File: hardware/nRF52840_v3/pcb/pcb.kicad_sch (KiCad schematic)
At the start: 151 parts, among them SW1 SW_DIP_x01, SW2 SW_DIP_x01, Y1 32.768 kHz

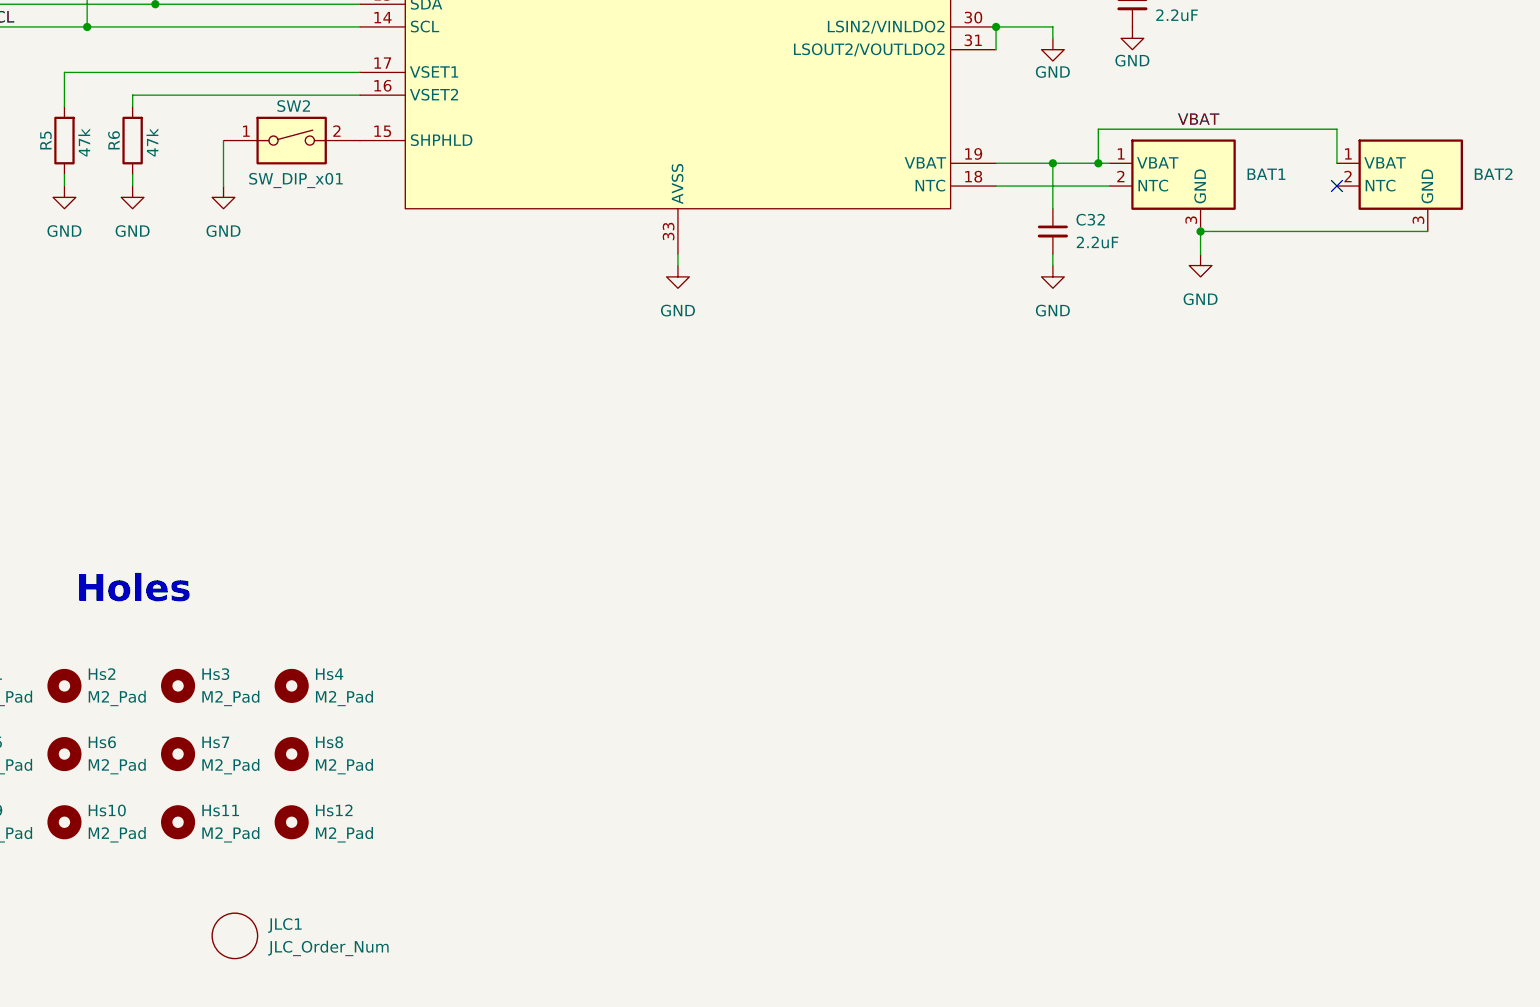
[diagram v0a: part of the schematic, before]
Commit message: M  hardware/nRF52840_v2/plate/plate.kicad_pcb M  hardware/nRF52840_v2/plate/plate.kicad_prl M  hardware/nRF52840_v2/plate/plate.kicad_pro A  hardware/nRF52840_v2/tmr-footprints/MountingHole_1.8mm_M1.6_NoPad.kicad_mod A  hardware/nRF52840_v2/tmr-footprints/MountingHole_2.2mm_M2.kicad_mod A  hardware/nRF52840_v2/tmr-footprints/SMTSO_M2.kicad_mod M  hardware/nRF52840_v3/border.py M  hardware/nRF52840_v3/pcb/pcb.kicad_pcb M  hardware/nRF52840_v3/pcb/pcb.kicad_prl M  hardware/nRF52840_v3/pcb/pcb.kicad_sch M  hardware/nRF52840_v3/placefp.py R  hardware/nRF52840_v2/plate/plate-Edge_Cuts.dxf -> hardware/nRF52840_v3/plate/plate-Edge_Cuts.dxf M  hardware/nRF52840_v3/plate/plate.kicad_pcb M  hardware/nRF52840_v3/plate/plate.kicad_prl M  hardware/nRF52840_v3/plate/plate.kicad_pro M  hardware/nRF52840_v3/plate/plate.kicad_sch A  hardware/nRF52840_v3/tmr-footprints/Aliexpress_SW_TACT_4x4x1.5mm.kicad_mod A  hardware/nRF52840_v3/tmr-footprints/MountingHole_1.8mm_M1.6_NoPad.kicad_mod A  hardware/nRF52840_v3/tmr-footprints/SMTSO_M2.kicad_mod M  hardware/nRF52840_v3/tmr-footprints/Stabilizer_Lowpro_2U.kicad_mod A  hardware/nRF52840_v3/tmr-footprints/USB_C_Receptacle_GCT_USB4085.kicad_mod
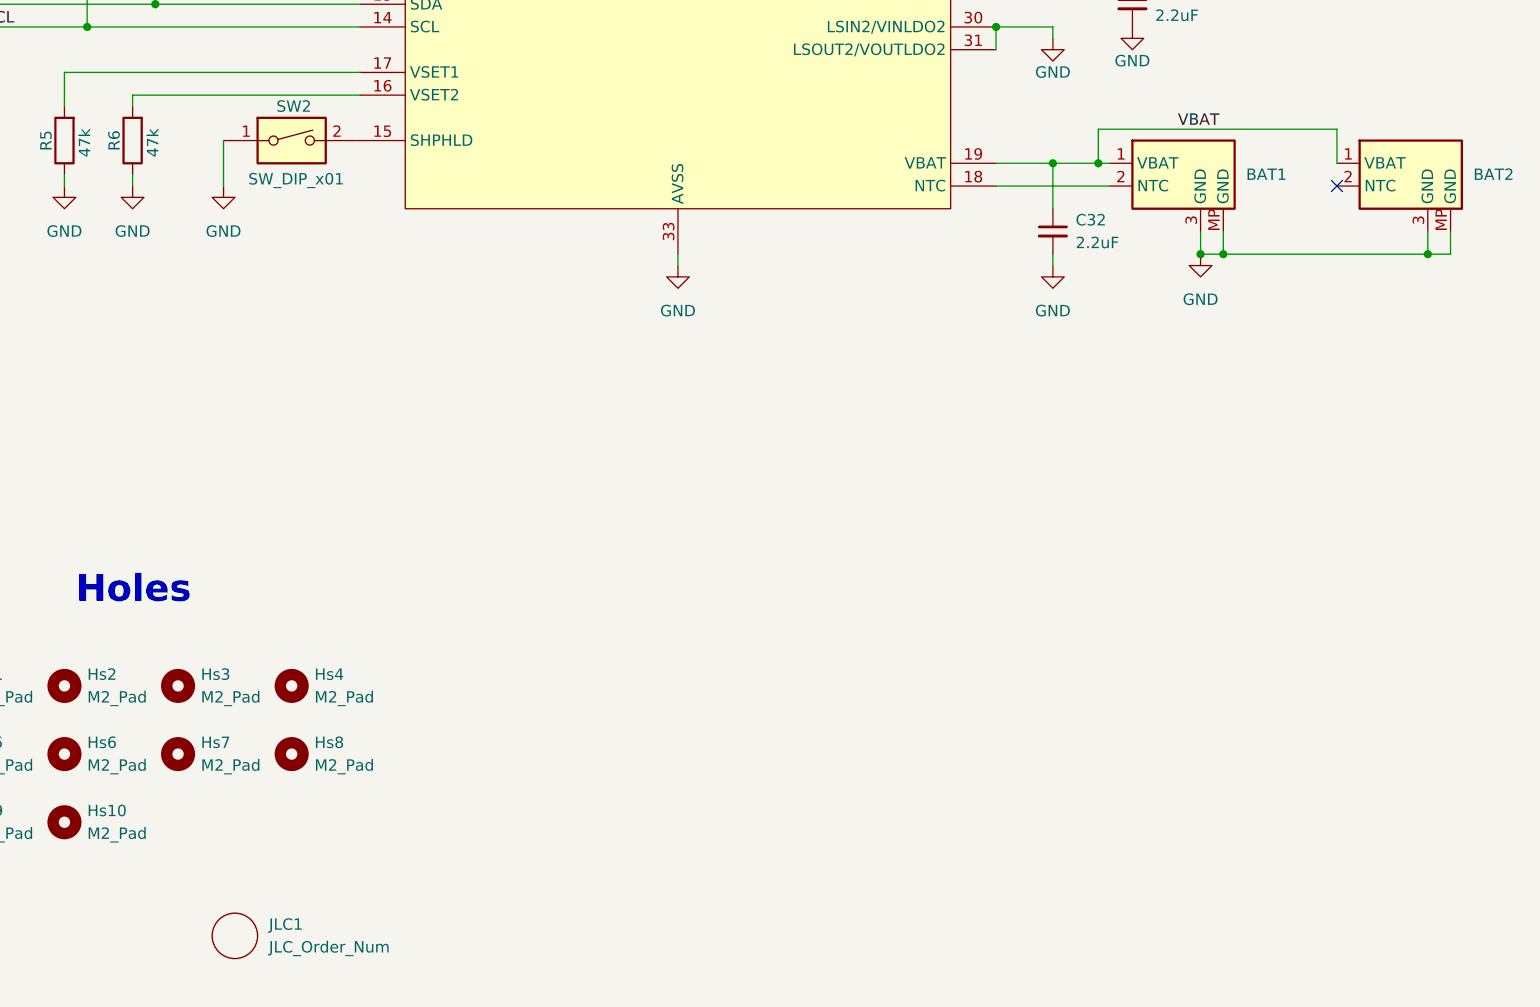
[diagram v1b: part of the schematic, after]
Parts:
- removed Hs11, Hs12: M2_Pad, MountingHole:MountingHole_2.2mm_M2_ISO7380_Pad_TopBottom, symbol Mechanical:MountingHole
- Hs1, Hs10, Hs2, Hs3, Hs4, Hs5, Hs6, Hs7, Hs8, Hs9: footprint MountingHole:MountingHole_2.2mm_M2_ISO7380_Pad_TopBottom -> tmr-lib:SMTSO_M1.6
- Jusb1: footprint tmr-lib:GCT_USB4215-03-A_REVA -> tmr-lib:USB_C_Receptacle_GCT_USB4085; ALTIUM_VALUE U262-161N-4BVC11 -> (none); LCSC C319148 -> (none); MANUFACTURER XKB Connectivity -> (none); MPN U262-161N-4BVC11 -> (none)
- SW1, SW2: footprint tmr-lib:Aliexpress_SW_DIP_TS_1292V_4x6.2x1.8mm -> tmr-lib:Aliexpress_SW_TACT_4x4x1.5mm
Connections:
- net GND: now also BAT1.MP (GND), BAT2.MP (GND)
